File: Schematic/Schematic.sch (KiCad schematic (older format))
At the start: 0 parts

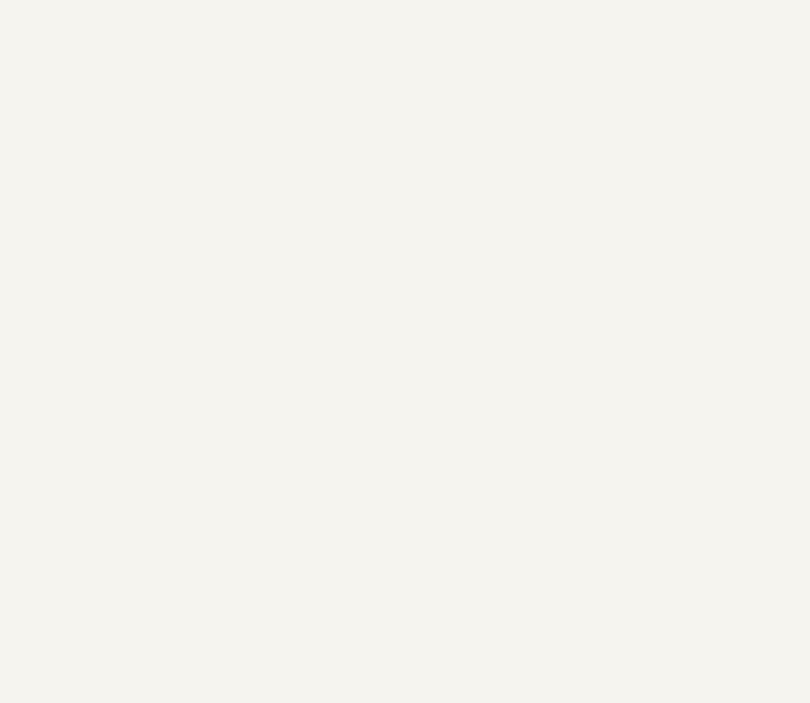
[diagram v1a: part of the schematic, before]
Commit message: Added a reset circuit and a single-step clock circuit to the schematic, as well as the bypass capacitors. Also, got used to the PCB creation workflow.
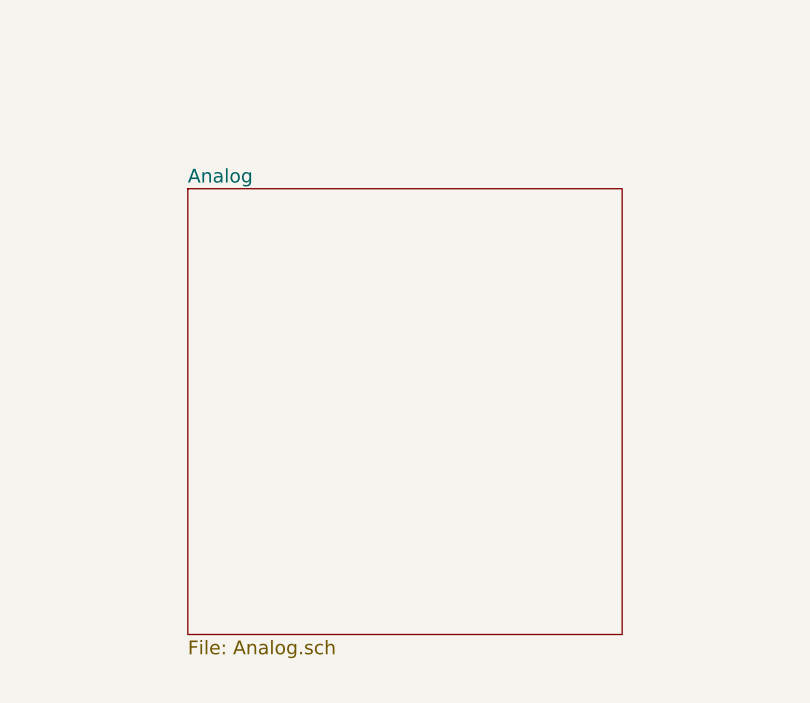
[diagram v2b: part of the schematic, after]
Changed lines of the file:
@@
 $Descr A4 11693 8268
 encoding utf-8
-Sheet 1 5
+Sheet 1 6
 Title ""
 Date ""
@@
 F1 "IR_Decode.sch" 60
 $EndSheet
+$Sheet
+S 4850 4000 1900 1950
+U 5C9C00CC
+F0 "Analog" 60
+F1 "Analog.sch" 60
+$EndSheet
 $EndSCHEMATC

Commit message: Brought the schematic and PCB board design up to date.
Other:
- note added: "ALU, A and B registers"
- note added: "Clock generation,\nreset generation,\nbypass capacitors,\nmisc. components"
- note added: "Instruction register,\nMicrosequencer,\nDecode logic and\ndemultiplexers"
- note added: "PC, Address Register\nand Jump Logic"
- note added: "RAM, ROM and UART"
